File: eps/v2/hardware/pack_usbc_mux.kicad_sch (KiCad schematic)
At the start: 22 parts, among them U2 TPS259470ARPW, U3 TPS259470ARPW

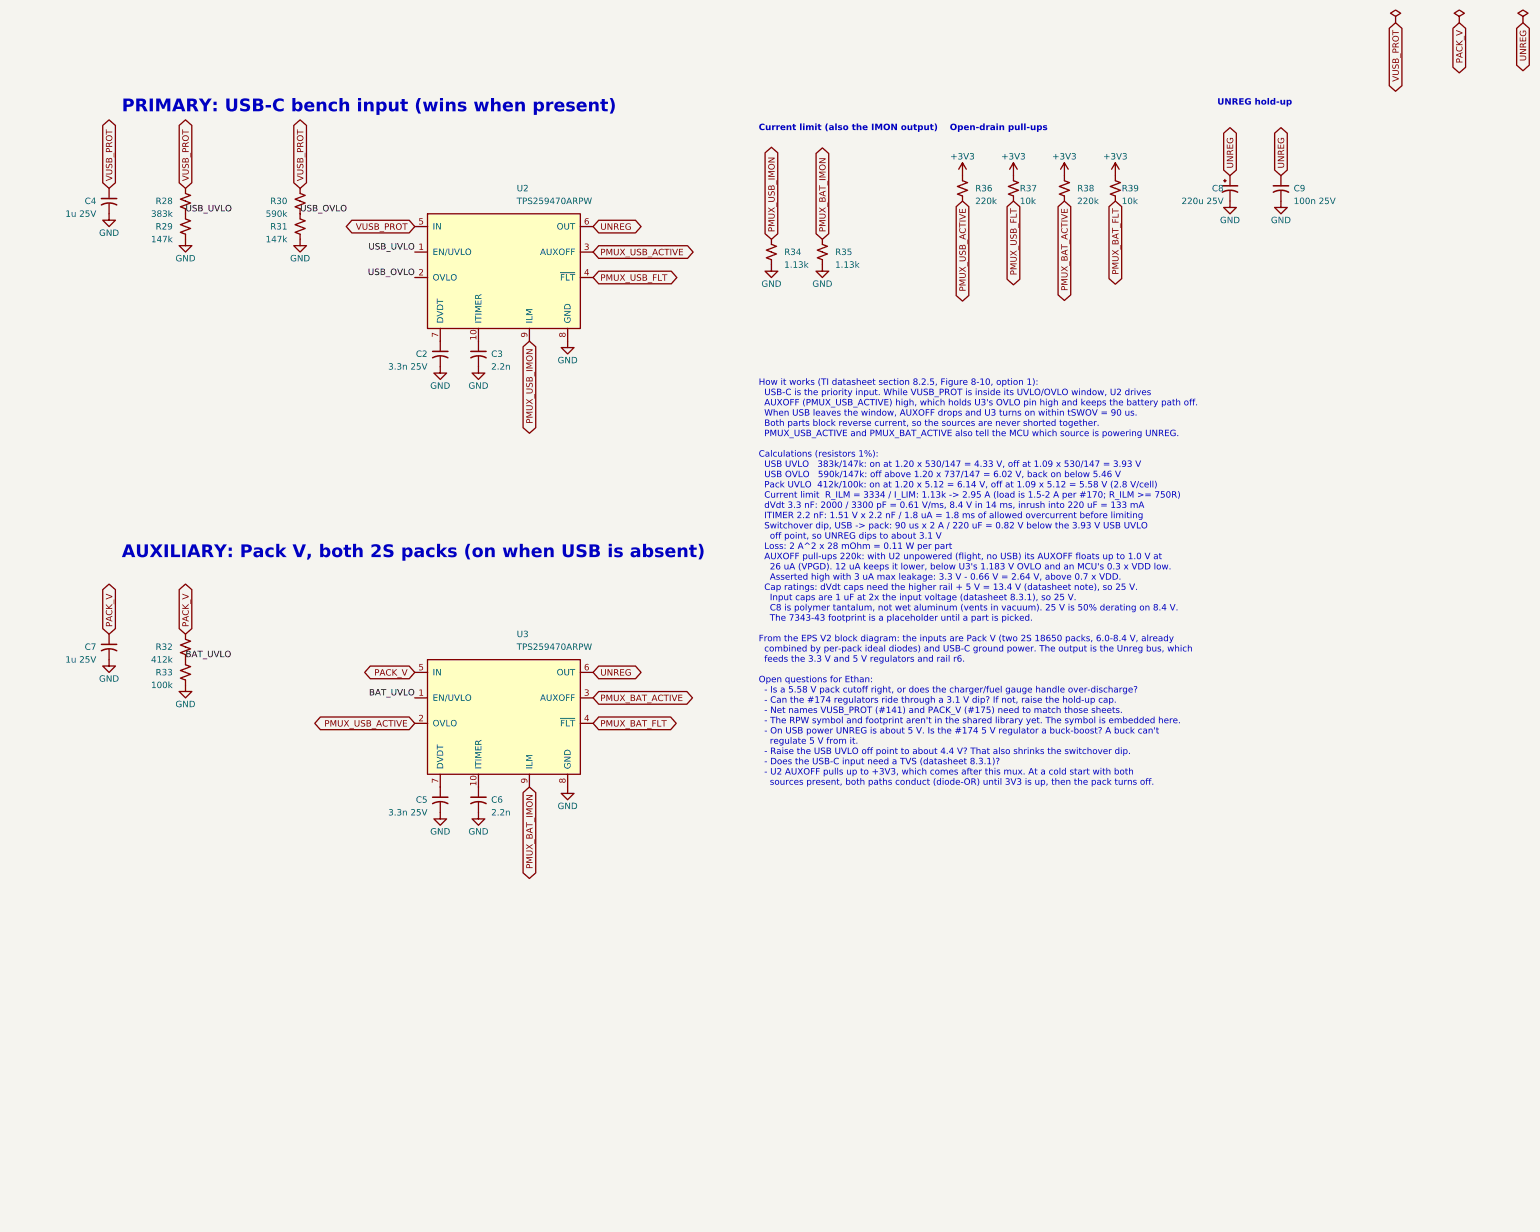
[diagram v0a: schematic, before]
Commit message: revise mux & create skeleton
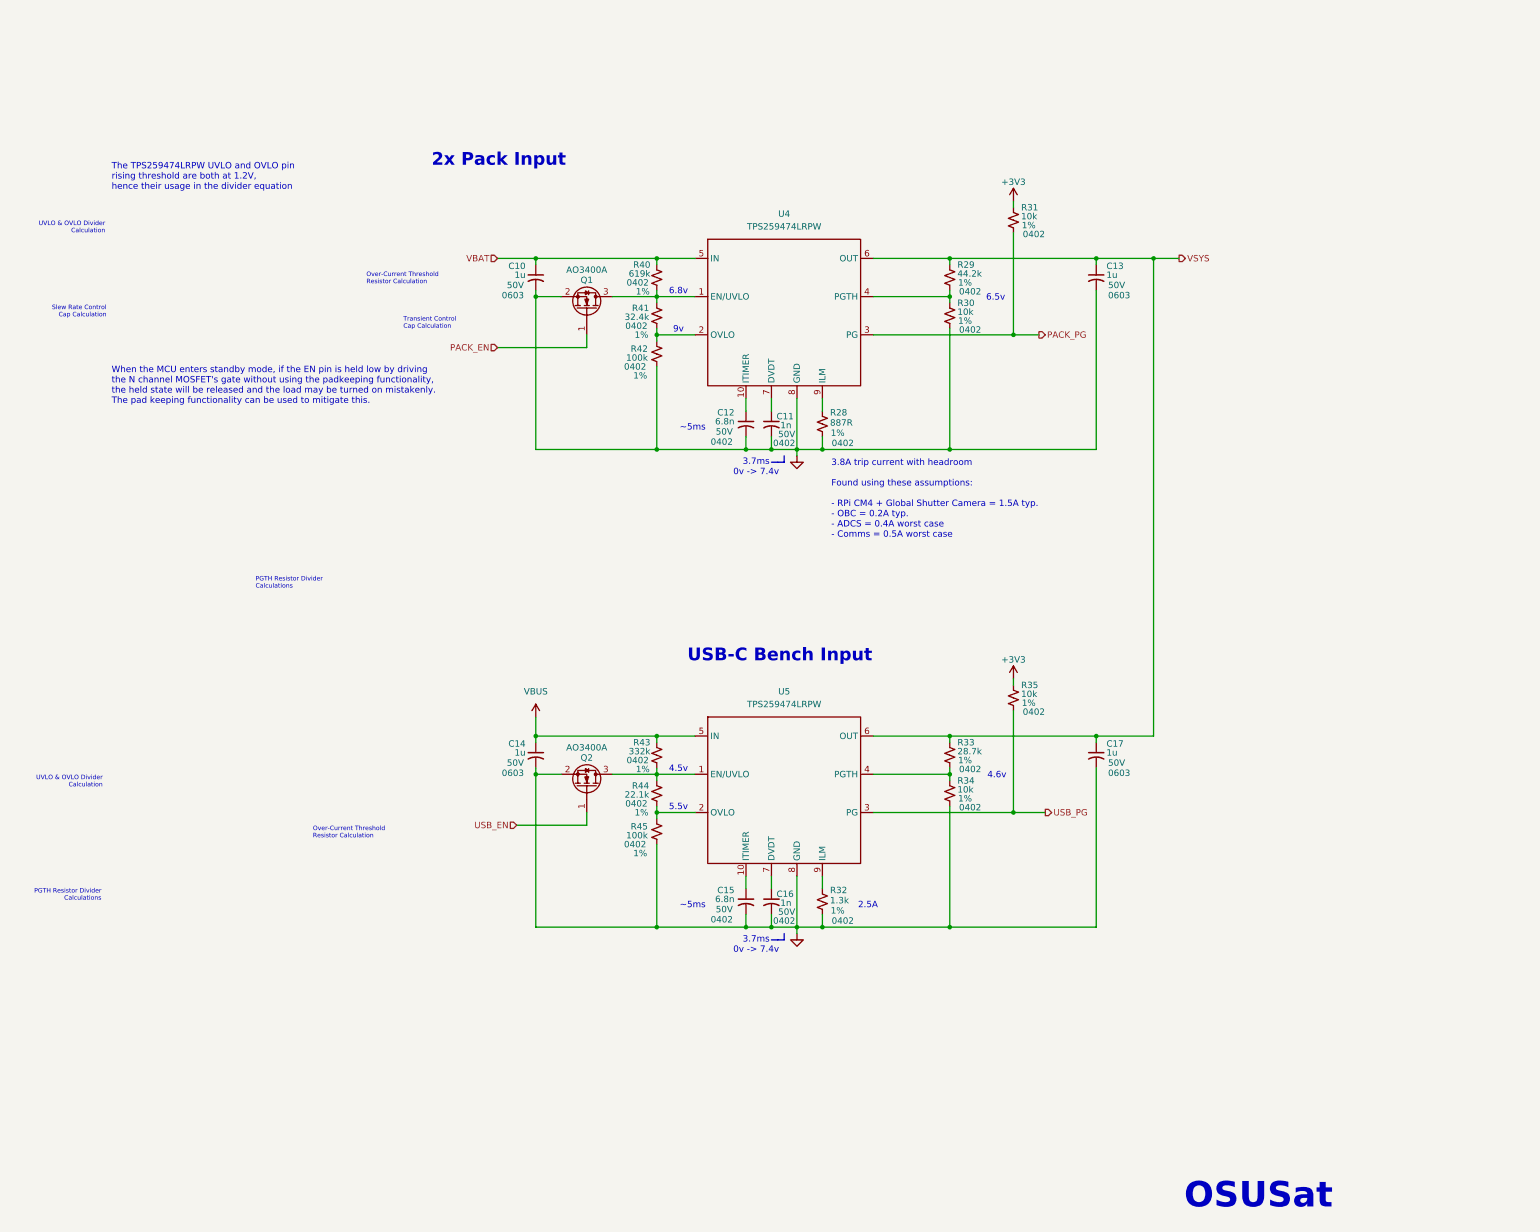
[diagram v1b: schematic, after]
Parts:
- removed C2, C5: 3.3n 25V, Capacitor_SMD:C_0603_1608Metric, symbol Device:C_Small_US
- removed C3, C6: 2.2n, Capacitor_SMD:C_0603_1608Metric, symbol Device:C_Small_US
- removed C4, C7: 1u 25V, Capacitor_SMD:C_0603_1608Metric, symbol Device:C_Small_US
- removed C8: 220u 25V, Capacitor_Tantalum_SMD:CP_EIA-7343-43_Kemet-X, symbol Device:C_Polarized_Small_US
- removed C9: 100n 25V, Capacitor_SMD:C_0603_1608Metric, symbol Device:C_Small_US
- removed R36, R38: 220k, Resistor_SMD:R_0603_1608Metric, symbol Device:R_Small_US
- removed R37, R39: 10k, Resistor_SMD:R_0603_1608Metric, symbol Device:R_Small_US
- removed U2, U3: TPS259470ARPW, symbol OSUSAT_EPS:TPS259470ARPW
- added C10, C13, C14, C17: 1u, Capacitor_SMD:C_0603_1608Metric, symbol Device:C_Small_US
- added C11, C16: 1n, Capacitor_SMD:C_0402_1005Metric, symbol Device:C_Small_US
- added C12, C15: 6.8n, Capacitor_SMD:C_0402_1005Metric, symbol Device:C_Small_US
- added Q1, Q2: AO3400A, Package_TO_SOT_SMD:SOT-23, symbol Transistor_FET:AO3400A
- added R40: 619k, Resistor_SMD:R_0603_1608Metric, symbol Device:R_Small_US
- added R41: 32.4k, Resistor_SMD:R_0603_1608Metric, symbol Device:R_Small_US
- added R42, R45: 100k, Resistor_SMD:R_0603_1608Metric, symbol Device:R_Small_US
- added R43: 332k, Resistor_SMD:R_0603_1608Metric, symbol Device:R_Small_US
- added R44: 22.1k, Resistor_SMD:R_0603_1608Metric, symbol Device:R_Small_US
- added U4, U5: TPS259474LRPW, OSUSAT_ICs:TPS2594x, symbol OSUSAT_EPS:TPS25947LRPW
- R28: value 383k -> 887R; footprint Resistor_SMD:R_0603_1608Metric -> Resistor_SMD:R_0402_1005Metric; LCSC PN (none) -> C4012675; Package (none) -> 0402; Tolerance (none) -> 1%
- R29: value 147k -> 44.2k; footprint Resistor_SMD:R_0603_1608Metric -> Resistor_SMD:R_0402_1005Metric; Package (none) -> 0402; Tolerance (none) -> 1%
- R30: value 590k -> 10k; footprint Resistor_SMD:R_0603_1608Metric -> Resistor_SMD:R_0402_1005Metric; Package (none) -> 0402; Tolerance (none) -> 1%
- R31: value 147k -> 10k; footprint Resistor_SMD:R_0603_1608Metric -> Resistor_SMD:R_0402_1005Metric; Package (none) -> 0402; Tolerance (none) -> 1%
- R32: value 412k -> 1.3k; footprint Resistor_SMD:R_0603_1608Metric -> Resistor_SMD:R_0402_1005Metric; LCSC PN (none) -> C4012675; Package (none) -> 0402; Tolerance (none) -> 1%
- R33: value 100k -> 28.7k; footprint Resistor_SMD:R_0603_1608Metric -> Resistor_SMD:R_0402_1005Metric; Package (none) -> 0402; Tolerance (none) -> 1%
- R34, R35: value 1.13k -> 10k; footprint Resistor_SMD:R_0603_1608Metric -> Resistor_SMD:R_0402_1005Metric; Package (none) -> 0402; Tolerance (none) -> 1%
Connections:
- net PMUX_BAT_IMON is gone; now on net +3V3: R35.1
- net +3V3: now also R31.1
- net GND: now also R28.2, R30.2, R32.2, C10.2, C11.2, C12.2, C13.2, C14.2, C15.2, C16.2, C17.2, Q1.2 (S), Q2.2 (S), R42.2, R45.2, U4.8 (GND), U5.8 (GND); no longer R29.2, R31.2, R33.2, R35.2
- net BAT_UVLO renamed VSYS
- net VSYS: now also R29.1, C13.1, C17.1, U4.6 (OUT), U5.6 (OUT); no longer R32.2
- net PACK_V: no longer names the net of R32.1
- net PACK_V: now also U5.9 (ILM)
- net PMUX_USB_IMON: no longer names the net of R34.1
- net PMUX_USB_IMON: now also R33.2, U5.4 (PGTH)
- removed net USB_OVLO: R30.2, R31.1
- removed net USB_UVLO: R28.2, R29.1
- net VUSB_PROT: no longer names the net of R30.1
- net VUSB_PROT: now also R29.2, U4.4 (PGTH); no longer R28.1
- new net: Q1.3 (D), R40.2, R41.1, U4.1 (EN/UVLO)
- new net: R41.2, R42.1, U4.2 (OVLO)
- new net: C11.1, U4.7 (DVDT)
- new net: C15.1, U5.10 (ITIMER)
- new net: Q2.3 (D), R43.2, R44.1, U5.1 (EN/UVLO)
- new net: R44.2, R45.1, U5.2 (OVLO)
- new net: C16.1, U5.7 (DVDT)
- new net: C12.1, U4.10 (ITIMER)
- new net: R28.1, U4.9 (ILM)
- new net PACK_EN: Q1.1 (G)
- new net PACK_PG: R31.2, U4.3 (PG)
- new net USB_EN: Q2.1 (G)
- new net USB_PG: R35.2, U5.3 (PG)
- new net VBAT: C10.1, R40.1, U4.5 (IN)
- new net VBUS: C14.1, R43.1, U5.5 (IN)
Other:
- note added: "2.5A"
- note added: "2x Pack Input"
- note added: "3.7ms 0v -> 7.4v"
- note added: "3.8A trip current with headroom Found using these assumptions: - RPi CM4 + Global Shutter Camera = 1.5A typ. - OBC = 0.2A typ. - ADCS = 0.4A worst case - Comms = 0.5A worst case"
- note added: "4.5v"
- note added: "4.6v"
- note added: "5.5v"
- note added: "6.5v"
- note added: "6.8v"
- note added: "9v"
- note added: "OSUSat"
- note added: "Over-Current Threshold Resistor Calculation"
- note added: "PGTH Resistor Divider Calculations"
- note added: "Slew Rate Control Cap Calculation"
- note added: "The TPS259474LRPW UVLO and OVLO pin rising threshold are both at 1.2V, hence their usage in the divider equation"
- note added: "Transient Control Cap Calculation"
- note added: "USB-C Bench Input"
- note added: "UVLO & OVLO Divider Calculation"
- note added: "When the MCU enters standby mode, if the EN pin is held low by driving the N channel MOSFET's gate without using the padkeeping functionality, the held state will be released and the load may be turned on mistakenly. The pad keeping functionality can be used to mitigate this."
- note added: "~5ms"
- note removed: "AUXILIARY: Pack V, both 2S packs (on when USB is absent)"
- note removed: "Current limit (also the IMON output)"
- note removed: "How it works (TI datasheet section 8.2.5, Figure 8-10, option 1): USB-C is the priority input. While VUSB_PROT is inside its UVLO/OVLO window, U2 drives AUXOFF (PMUX_USB_ACTIVE) high, which holds U3's OVLO pin high and keeps the battery path off. When USB leaves the window, AUXOFF drops and U3 turns on within tSWOV = 90 us. Both parts block reverse current, so the sources are never shorted togeth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"
- note removed: "Open-drain pull-ups"
- note removed: "PRIMARY: USB-C bench input (wins when present)"
- note removed: "UNREG hold-up"

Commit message: Finish #173 mux and rebuild #178 as rail eFuse EN control
#173: Q1/Q2 gate pull-downs, test points on VSYS and both PGs, FET MPN/LCSC, R40-45 footprints to 0402, pin 6 ERC exclusion.

#178: replace the TCA9548A sheet with 8 FET EN/UVLO pull-downs and boot-default gate pulls (r1 on, r2-r8 off), drawn in the #173 style. Sheet pins added on the top level, calc images.

Add TPS25947 and AO3400A datasheets.
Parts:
- added R46, R47: 100k, Resistor_SMD:R_0402_1005Metric, symbol Device:R_Small_US
- added TP1: PACK_PG, TestPoint:TestPoint_Pad_D1.0mm, symbol Connector:TestPoint
- added TP2: USB_PG, TestPoint:TestPoint_Pad_D1.0mm, symbol Connector:TestPoint
- added TP3: VSYS, TestPoint:TestPoint_Pad_D1.0mm, symbol Connector:TestPoint
- Q1, Q2: LCSC (none) -> C20917; MPN (none) -> AO3400A
- R40, R41, R42, R43, R44, R45: footprint Resistor_SMD:R_0603_1608Metric -> Resistor_SMD:R_0402_1005Metric
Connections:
- net GND: now also R46.2, R47.2
- net PACK_EN: now also R46.1
- net PACK_PG: now also TP1.1
- net USB_EN: now also R47.1
- net USB_PG: now also TP2.1
- net VSYS: now also TP3.1
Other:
- note added: "2.5ms 0v -> 5v"
